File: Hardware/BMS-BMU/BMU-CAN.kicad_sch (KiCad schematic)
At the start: 0 parts

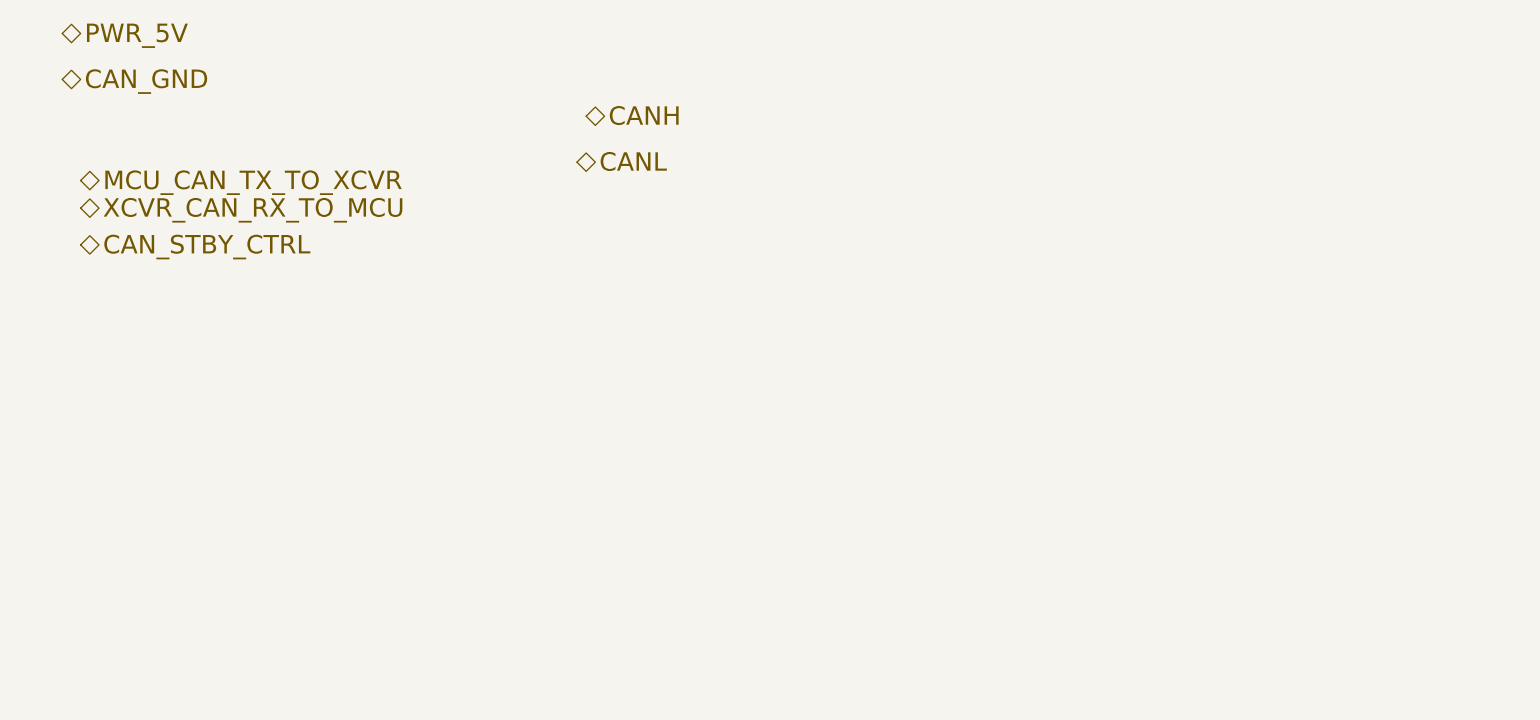
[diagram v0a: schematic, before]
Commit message: update CAN and SHUNT IF
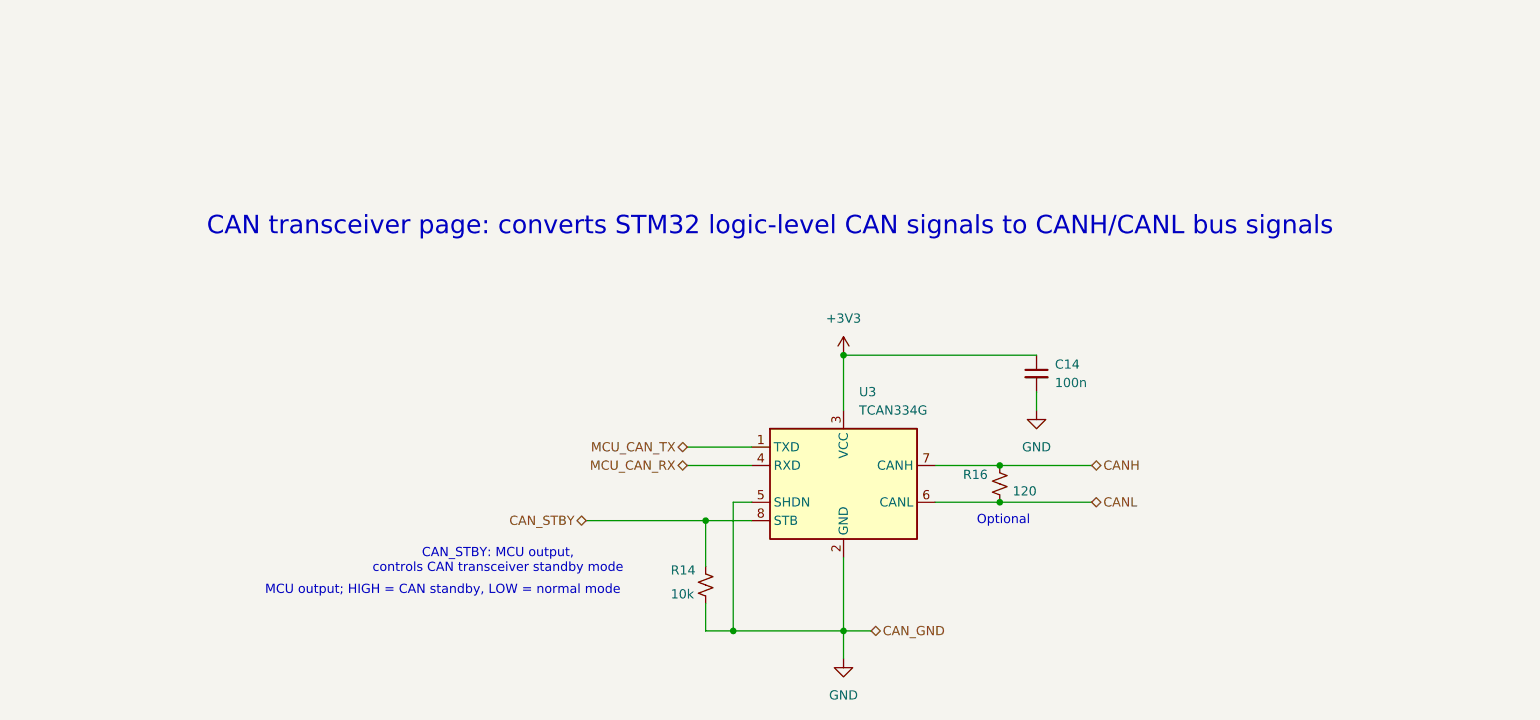
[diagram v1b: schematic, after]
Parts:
- added C14: 100n, symbol Device:C_Small
- added R14: 10k, symbol Device:R_Small_US
- added R16: 120, symbol Device:R_Small_US
- added U3: TCAN334G, symbol Interface_CAN_LIN:TCAN334G
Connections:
- net CANH: now also R16.1, U3.7 (CANH)
- net CANL: now also R16.2, U3.6 (CANL)
- new net +3V3: C14.1, U3.3 (VCC)
- new net CAN_STBY: R14.1, U3.8 (STB)
- new net GND: C14.2, R14.2, U3.2 (GND), U3.5 (SHDN)
- new net MCU_CAN_RX: U3.4 (RXD)
- new net MCU_CAN_TX: U3.1 (TXD)
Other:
- note added: "CAN transceiver page: converts STM32 logic-level CAN signals to CANH/CANL bus signals"
- note added: "CAN_STBY: MCU output, controls CAN transceiver standby mode"
- note added: "MCU output; HIGH = CAN standby, LOW = normal mode"
- note added: "Optional"
